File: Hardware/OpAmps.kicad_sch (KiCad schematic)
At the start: 60 parts

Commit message: Started laying out component PCB
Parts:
- added C37, C38, C39, C40, C41, C42, C43, C44, C45, C46: 100nF, Capacitor_SMD:C_0603_1608Metric, symbol Device:C_Small
- added unit 5 of U10
- added unit 5 of U11
- added unit 5 of U12
- added unit 5 of U13
- added unit 5 of U14
- R36, R37, R38, R39, R40, R41, R42, R43, R44, R45, R46, R47, R48, R49, R50, R51: renamed from R?; footprint Resistors_SMD:R_0805_HandSoldering -> Resistor_SMD:R_0603_1608Metric
- R52, R53, R54, R55, R56, R57, R58, R59, R60, R61, R62, R63, R64, R65, R66, R67, R68, R69, R70, R71, R72, R73, R74, R75: renamed from R?; footprint Resistor_SMD:R_0603_1608Metric_Pad0.98x0.95mm_HandSolder -> Resistor_SMD:R_0603_1608Metric
- U10, U11: renamed from U?; footprint SMD_Packages:SOIC-14_N -> Package_SO:SOIC-14_3.9x8.7mm_P1.27mm
- gave numbers to parts that had none: 3
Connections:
- net GND: now also C37.2, C38.2, C39.2, C40.2, C41.2, C42.2, C43.2, C44.2, C45.2, C46.2
- new net +12V: C37.1, C39.1, C41.1, C43.1, C45.1, U10.4 (V+), U11.4 (V+), U12.11 (V-), U13.11 (V-), U14.11 (V-)
- new net -12V: C38.1, C40.1, C42.1, C44.1, C46.1, U10.11 (V-), U11.11 (V-), U12.4 (V+), U13.4 (V+), U14.4 (V+)

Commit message: Started op-amp layout
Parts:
- U10, U11, U12, U13, U14: footprint Package_SO:SOIC-14_3.9x8.7mm_P1.27mm -> Package_SO:TSSOP-14_4.4x5mm_P0.65mm
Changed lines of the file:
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@@
     (property "Reference" "U12" (id 0) (at 171.45 31.75 0))
     (property "Value" "TL074" (id 1) (at 171.45 39.37 0))
-    (property "Footprint" "Package_SO:SOIC-14_3.9x8.7mm_P1.27mm" (id 2) (at 167.64 38.1 0)
+    (property "Footprint" "Package_SO:TSSOP-14_4.4x5mm_P0.65mm" (id 2) (at 167.64 38.1 0)
       (effects (font (size 1.27 1.27)) hide)
     )
@@
     (property "Reference" "U12" (id 0) (at 172.72 96.52 0))
     (property "Value" "TL074" (id 1) (at 172.72 104.14 0))
-    (property "Footprint" "Package_SO:SOIC-14_3.9x8.7mm_P1.27mm" (id 2) (at 168.91 102.87 0)
+    (property "Footprint" "Package_SO:TSSOP-14_4.4x5mm_P0.65mm" (id 2) (at 168.91 102.87 0)
       (effects (font (size 1.27 1.27)) hide)
     )
@@
     (property "Reference" "U14" (id 0) (at 311.15 63.5 0))
     (property "Value" "TL074" (id 1) (at 311.15 71.12 0))
-    (property "Footprint" "Package_SO:SOIC-14_3.9x8.7mm_P1.27mm" (id 2) (at 307.34 69.85 0)
+    (property "Footprint" "Package_SO:TSSOP-14_4.4x5mm_P0.65mm" (id 2) (at 307.34 69.85 0)
       (effects (font (size 1.27 1.27)) hide)
     )
@@
     (property "Reference" "U11" (id 0) (at 100.33 57.9882 0))
     (property "Value" "TL074" (id 1) (at 100.33 60.2996 0))
-    (property "Footprint" "Package_SO:SOIC-14_3.9x8.7mm_P1.27mm" (id 2) (at 99.06 64.77 0)
+    (property "Footprint" "Package_SO:TSSOP-14_4.4x5mm_P0.65mm" (id 2) (at 99.06 64.77 0)
       (effects (font (size 1.27 1.27)) hide)
     )
@@
     (property "Reference" "U11" (id 0) (at 96.52 182.4482 0))
     (property "Value" "TL074" (id 1) (at 96.52 184.7596 0))
-    (property "Footprint" "Package_SO:SOIC-14_3.9x8.7mm_P1.27mm" (id 2) (at 95.25 189.23 0)
+    (property "Footprint" "Package_SO:TSSOP-14_4.4x5mm_P0.65mm" (id 2) (at 95.25 189.23 0)
       (effects (font (size 1.27 1.27)) hide)
     )
@@
     (property "Reference" "U10" (id 0) (at 44.45 122.7582 0))
     (property "Value" "TL074" (id 1) (at 44.45 125.0696 0))
-    (property "Footprint" "Package_SO:SOIC-14_3.9x8.7mm_P1.27mm" (id 2) (at 43.18 129.54 0)
+    (property "Footprint" "Package_SO:TSSOP-14_4.4x5mm_P0.65mm" (id 2) (at 43.18 129.54 0)
       (effects (font (size 1.27 1.27)) hide)
     )
@@
     (property "Reference" "U10" (id 0) (at 44.45 26.2382 0))
     (property "Value" "TL074" (id 1) (at 44.45 28.5496 0))
-    (property "Footprint" "Package_SO:SOIC-14_3.9x8.7mm_P1.27mm" (id 2) (at 43.18 33.02 0)
+    (property "Footprint" "Package_SO:TSSOP-14_4.4x5mm_P0.65mm" (id 2) (at 43.18 33.02 0)
       (effects (font (size 1.27 1.27)) hide)
     )
@@
     (property "Reference" "U12" (id 0) (at 172.72 63.5 0))
     (property "Value" "TL074" (id 1) (at 172.72 71.12 0))
-    (property "Footprint" "Package_SO:SOIC-14_3.9x8.7mm_P1.27mm" (id 2) (at 168.91 69.85 0)
+    (property "Footprint" "Package_SO:TSSOP-14_4.4x5mm_P0.65mm" (id 2) (at 168.91 69.85 0)
       (effects (font (size 1.27 1.27)) hide)
     )
@@
     (property "Reference" "U13" (id 0) (at 231.14 96.52 0))
     (property "Value" "TL074" (id 1) (at 231.14 104.14 0))
-    (property "Footprint" "Package_SO:SOIC-14_3.9x8.7mm_P1.27mm" (id 2) (at 227.33 102.87 0)
+    (property "Footprint" "Package_SO:TSSOP-14_4.4x5mm_P0.65mm" (id 2) (at 227.33 102.87 0)
       (effects (font (size 1.27 1.27)) hide)
     )
@@
     (property "Reference" "U13" (id 0) (at 229.87 31.75 0))
     (property "Value" "TL074" (id 1) (at 229.87 39.37 0))
-    (property "Footprint" "Package_SO:SOIC-14_3.9x8.7mm_P1.27mm" (id 2) (at 226.06 38.1 0)
+    (property "Footprint" "Package_SO:TSSOP-14_4.4x5mm_P0.65mm" (id 2) (at 226.06 38.1 0)
       (effects (font (size 1.27 1.27)) hide)
     )
@@
     (property "Reference" "U12" (id 0) (at 171.45 187.96 0))
     (property "Value" "TL074" (id 1) (at 171.45 195.58 0))
-    (property "Footprint" "Package_SO:SOIC-14_3.9x8.7mm_P1.27mm" (id 2) (at 167.64 194.31 0)
+    (property "Footprint" "Package_SO:TSSOP-14_4.4x5mm_P0.65mm" (id 2) (at 167.64 194.31 0)
       (effects (font (size 1.27 1.27)) hide)
     )
@@
     (property "Reference" "U11" (id 0) (at 100.33 91.0082 0))
     (property "Value" "TL074" (id 1) (at 100.33 93.3196 0))
-    (property "Footprint" "Package_SO:SOIC-14_3.9x8.7mm_P1.27mm" (id 2) (at 99.06 97.79 0)
+    (property "Footprint" "Package_SO:TSSOP-14_4.4x5mm_P0.65mm" (id 2) (at 99.06 97.79 0)
       (effects (font (size 1.27 1.27)) hide)
     )
@@
     (property "Reference" "U10" (id 0) (at 44.45 57.9882 0))
     (property "Value" "TL074" (id 1) (at 44.45 60.2996 0))
-    (property "Footprint" "Package_SO:SOIC-14_3.9x8.7mm_P1.27mm" (id 2) (at 43.18 64.77 0)
+    (property "Footprint" "Package_SO:TSSOP-14_4.4x5mm_P0.65mm" (id 2) (at 43.18 64.77 0)
       (effects (font (size 1.27 1.27)) hide)
     )
@@
       (effects (font (size 1.27 1.27)) (justify left))
     )
-    (property "Footprint" "Package_SO:SOIC-14_3.9x8.7mm_P1.27mm" (id 2) (at 39.37 190.5 0)
+    (property "Footprint" "Package_SO:TSSOP-14_4.4x5mm_P0.65mm" (id 2) (at 39.37 190.5 0)
       (effects (font (size 1.27 1.27)) hide)
     )
@@
     (property "Reference" "U14" (id 0) (at 306.07 185.42 0))
     (property "Value" "TL074" (id 1) (at 306.07 193.04 0))
-    (property "Footprint" "Package_SO:SOIC-14_3.9x8.7mm_P1.27mm" (id 2) (at 302.26 191.77 0)
+    (property "Footprint" "Package_SO:TSSOP-14_4.4x5mm_P0.65mm" (id 2) (at 302.26 191.77 0)
       (effects (font (size 1.27 1.27)) hide)
     )
@@
     (property "Reference" "U13" (id 0) (at 231.14 128.27 0))
     (property "Value" "TL074" (id 1) (at 231.14 135.89 0))
-    (property "Footprint" "Package_SO:SOIC-14_3.9x8.7mm_P1.27mm" (id 2) (at 227.33 134.62 0)
+    (property "Footprint" "Package_SO:TSSOP-14_4.4x5mm_P0.65mm" (id 2) (at 227.33 134.62 0)
       (effects (font (size 1.27 1.27)) hide)
     )
@@
     (property "Reference" "U13" (id 0) (at 231.14 63.5 0))
     (property "Value" "TL074" (id 1) (at 231.14 71.12 0))
-    (property "Footprint" "Package_SO:SOIC-14_3.9x8.7mm_P1.27mm" (id 2) (at 227.33 69.85 0)
+    (property "Footprint" "Package_SO:TSSOP-14_4.4x5mm_P0.65mm" (id 2) (at 227.33 69.85 0)
       (effects (font (size 1.27 1.27)) hide)
     )
@@
     (property "Reference" "U14" (id 0) (at 311.15 128.27 0))
     (property "Value" "TL074" (id 1) (at 311.15 135.89 0))
-    (property "Footprint" "Package_SO:SOIC-14_3.9x8.7mm_P1.27mm" (id 2) (at 307.34 134.62 0)
+    (property "Footprint" "Package_SO:TSSOP-14_4.4x5mm_P0.65mm" (id 2) (at 307.34 134.62 0)
       (effects (font (size 1.27 1.27)) hide)
     )
@@
     (property "Reference" "U13" (id 0) (at 232.41 186.69 0))
     (property "Value" "TL074" (id 1) (at 232.41 194.31 0))
-    (property "Footprint" "Package_SO:SOIC-14_3.9x8.7mm_P1.27mm" (id 2) (at 228.6 193.04 0)
+    (property "Footprint" "Package_SO:TSSOP-14_4.4x5mm_P0.65mm" (id 2) (at 228.6 193.04 0)
       (effects (font (size 1.27 1.27)) hide)
     )
@@
     (property "Reference" "U11" (id 0) (at 100.33 122.7582 0))
     (property "Value" "TL074" (id 1) (at 100.33 125.0696 0))
-    (property "Footprint" "Package_SO:SOIC-14_3.9x8.7mm_P1.27mm" (id 2) (at 99.06 129.54 0)
+    (property "Footprint" "Package_SO:TSSOP-14_4.4x5mm_P0.65mm" (id 2) (at 99.06 129.54 0)
       (effects (font (size 1.27 1.27)) hide)
     )
@@
     (property "Reference" "U11" (id 0) (at 100.33 26.2382 0))
     (property "Value" "TL074" (id 1) (at 100.33 28.5496 0))
-    (property "Footprint" "Package_SO:SOIC-14_3.9x8.7mm_P1.27mm" (id 2) (at 99.06 33.02 0)
+    (property "Footprint" "Package_SO:TSSOP-14_4.4x5mm_P0.65mm" (id 2) (at 99.06 33.02 0)
       (effects (font (size 1.27 1.27)) hide)
     )
@@
     (property "Reference" "U14" (id 0) (at 311.15 96.52 0))
     (property "Value" "TL074" (id 1) (at 311.15 104.14 0))
-    (property "Footprint" "Package_SO:SOIC-14_3.9x8.7mm_P1.27mm" (id 2) (at 307.34 102.87 0)
+    (property "Footprint" "Package_SO:TSSOP-14_4.4x5mm_P0.65mm" (id 2) (at 307.34 102.87 0)
       (effects (font (size 1.27 1.27)) hide)
     )
@@
     (property "Reference" "U14" (id 0) (at 309.88 31.75 0))
     (property "Value" "TL074" (id 1) (at 309.88 39.37 0))
-    (property "Footprint" "Package_SO:SOIC-14_3.9x8.7mm_P1.27mm" (id 2) (at 306.07 38.1 0)
+    (property "Footprint" "Package_SO:TSSOP-14_4.4x5mm_P0.65mm" (id 2) (at 306.07 38.1 0)
       (effects (font (size 1.27 1.27)) hide)
     )
@@
     (property "Reference" "U10" (id 0) (at 44.45 91.0082 0))
     (property "Value" "TL074" (id 1) (at 44.45 93.3196 0))
-    (property "Footprint" "Package_SO:SOIC-14_3.9x8.7mm_P1.27mm" (id 2) (at 43.18 97.79 0)
+    (property "Footprint" "Package_SO:TSSOP-14_4.4x5mm_P0.65mm" (id 2) (at 43.18 97.79 0)
       (effects (font (size 1.27 1.27)) hide)
     )
@@
     (property "Reference" "U12" (id 0) (at 172.72 128.27 0))
     (property "Value" "TL074" (id 1) (at 172.72 135.89 0))
-    (property "Footprint" "Package_SO:SOIC-14_3.9x8.7mm_P1.27mm" (id 2) (at 168.91 134.62 0)
-      (effects (font (size 1.27 1.27)) hide)
-    )
+    (property "Footprint" "Package_SO:TSSOP-14_4.4x5mm_P0.65mm" (id 2) (at 168.91 134.62 0)
+      (effects (font (size 1.27 1.27)) hide)
+    )

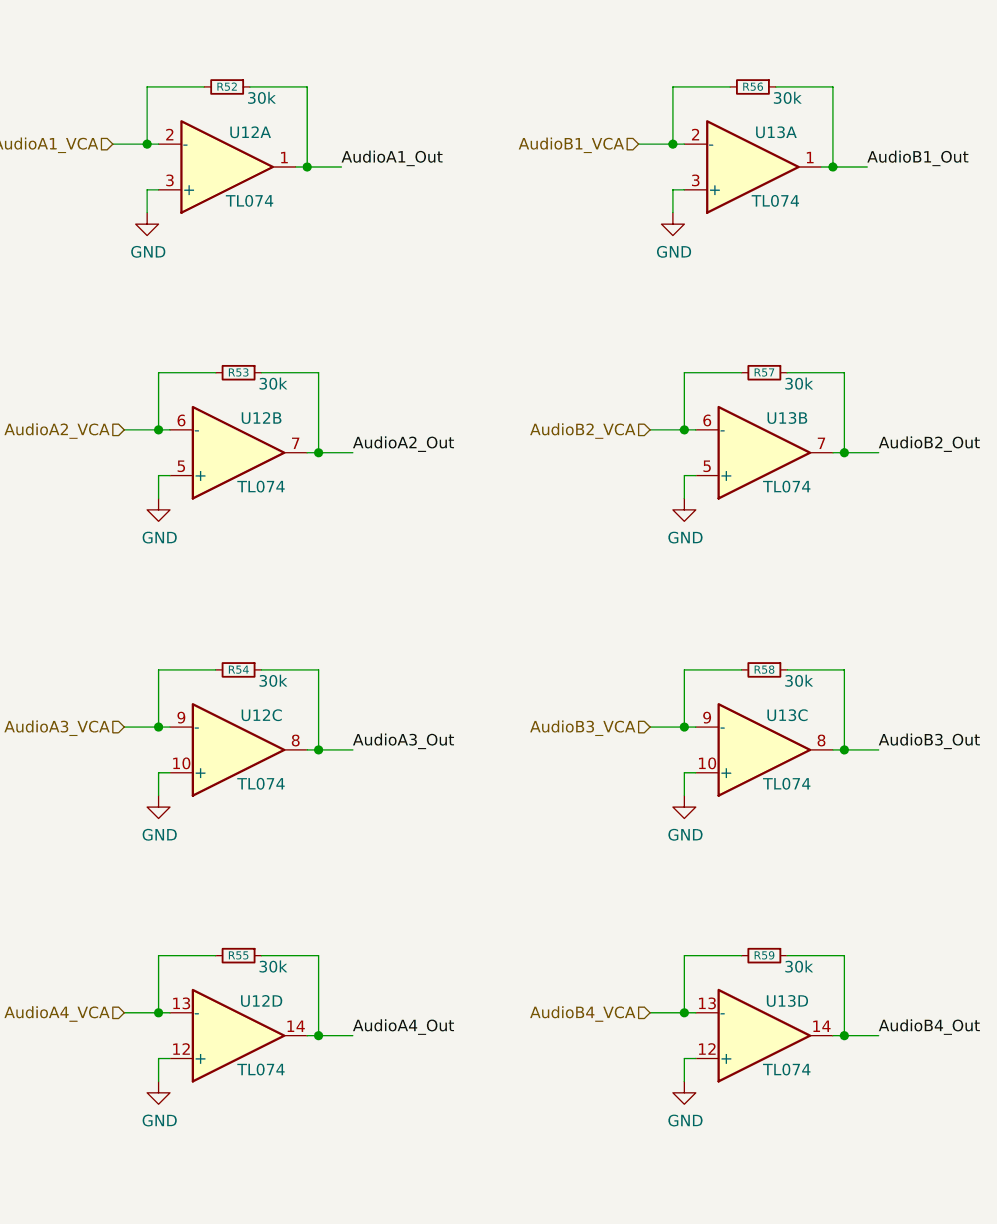
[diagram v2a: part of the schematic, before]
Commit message: Layout of audio vca section
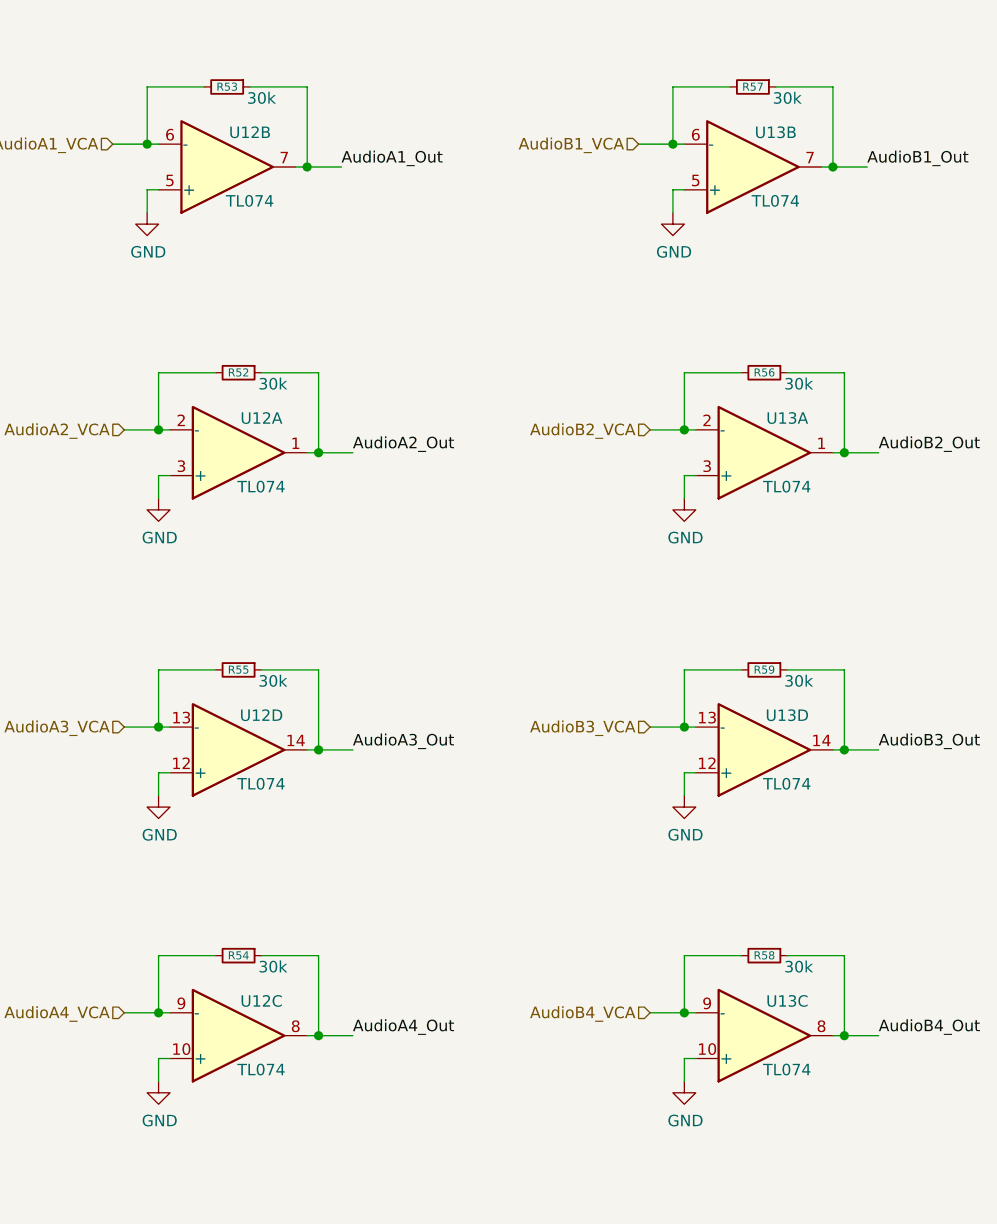
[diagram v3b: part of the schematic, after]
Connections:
- net AudioA1_Out: now also R53.1, U12.7; no longer R52.1, U12.1
- net AudioA1_VCA: now also R53.2, U12.6 (-); no longer R52.2, U12.2 (-)
- net AudioA2_Out: now also R52.1, U12.1; no longer R53.1, U12.7
- net AudioA2_VCA: now also R52.2, U12.2 (-); no longer R53.2, U12.6 (-)
- net AudioA3_Out: now also R55.1, U12.14; no longer R54.1, U12.8
- net AudioA3_VCA: now also R55.2, U12.13 (-); no longer R54.2, U12.9 (-)
- net AudioA4_Out: now also R54.1, U12.8; no longer R55.1, U12.14
- net AudioA4_VCA: now also R54.2, U12.9 (-); no longer R55.2, U12.13 (-)
- net AudioB1_Out: now also R57.1, U13.7; no longer R56.1, U13.1
- net AudioB1_VCA: now also R57.2, U13.6 (-); no longer R56.2, U13.2 (-)
- net AudioB2_Out: now also R56.1, U13.1; no longer R57.1, U13.7
- net AudioB2_VCA: now also R56.2, U13.2 (-); no longer R57.2, U13.6 (-)
- net AudioB3_Out: now also R59.1, U13.14; no longer R58.1, U13.8
- net AudioB3_VCA: now also R59.2, U13.13 (-); no longer R58.2, U13.9 (-)
- net AudioB4_Out: now also R58.1, U13.8; no longer R59.1, U13.14
- net AudioB4_VCA: now also R58.2, U13.9 (-); no longer R59.2, U13.13 (-)
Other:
- moved on the sheet: R52, R53, R54, R55, R56, R57, R58, R59, U12A, U12B, U12C, U12D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

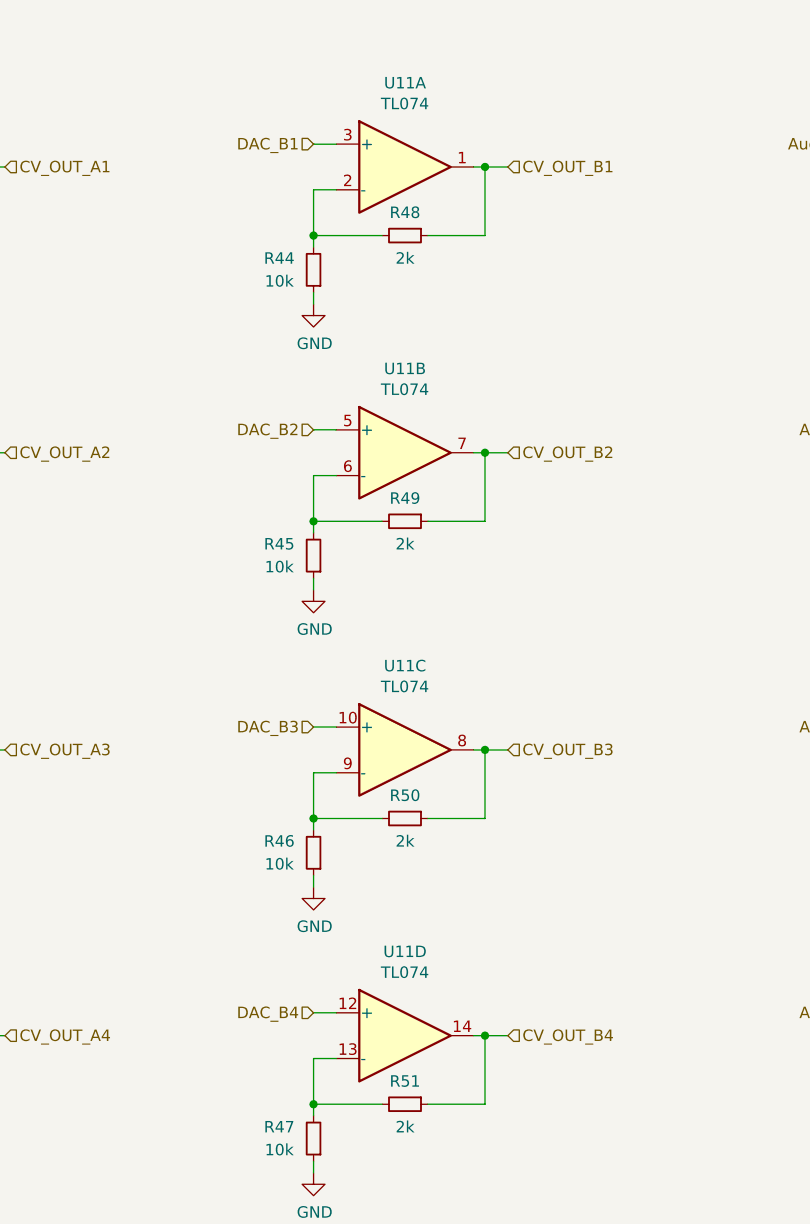
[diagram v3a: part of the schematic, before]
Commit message: Main components positioned
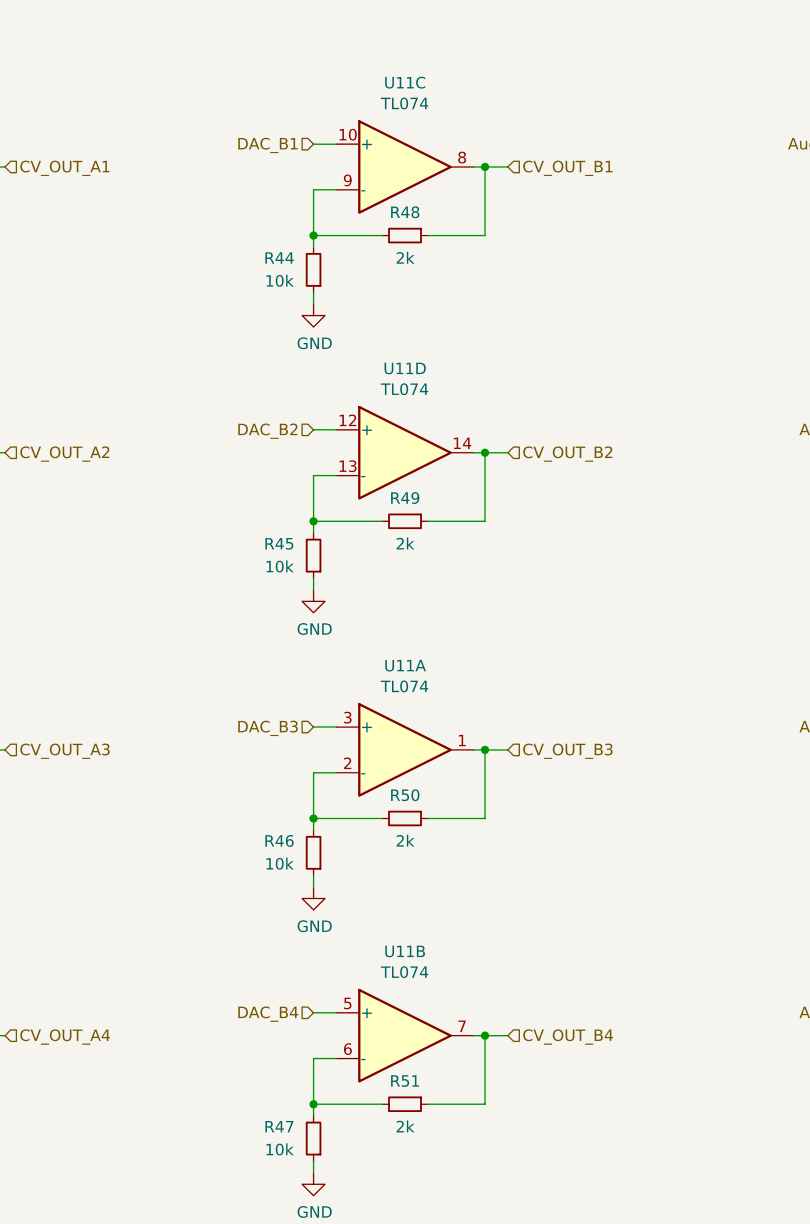
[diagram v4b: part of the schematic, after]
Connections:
- net CV_OUT_B1: now also U11.8; no longer U11.1
- net CV_OUT_B2: now also U11.14; no longer U11.7
- net CV_OUT_B3: now also U11.1; no longer U11.8
- net CV_OUT_B4: now also U11.7; no longer U11.14
- net DAC_B1: now also U11.10 (+); no longer U11.3 (+)
- net DAC_B2: now also U11.12 (+); no longer U11.5 (+)
- net DAC_B3: now also U11.3 (+); no longer U11.10 (+)
- net DAC_B4: now also U11.5 (+); no longer U11.12 (+)
- net at R46.2, R50.2: now also U11.2 (-); no longer U11.9 (-)
- net at R47.2, R51.2: now also U11.6 (-); no longer U11.13 (-)
- net at R45.2, R49.2: now also U11.13 (-); no longer U11.6 (-)
- net at R44.2, R48.2: now also U11.9 (-); no longer U11.2 (-)
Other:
- moved on the sheet: U11A, U11B, U11C, U11D
